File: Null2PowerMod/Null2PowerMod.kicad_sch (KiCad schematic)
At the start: 33 parts, among them J1 Conn_01x01, J2 USB_C_Receptacle_USB2.0, J3 Conn_01x01, J5 JST 2-PH, J6 Conn_01x01, U1 MCP73871, U2 TPS61030PWP, U3 MMUN2133LT1G

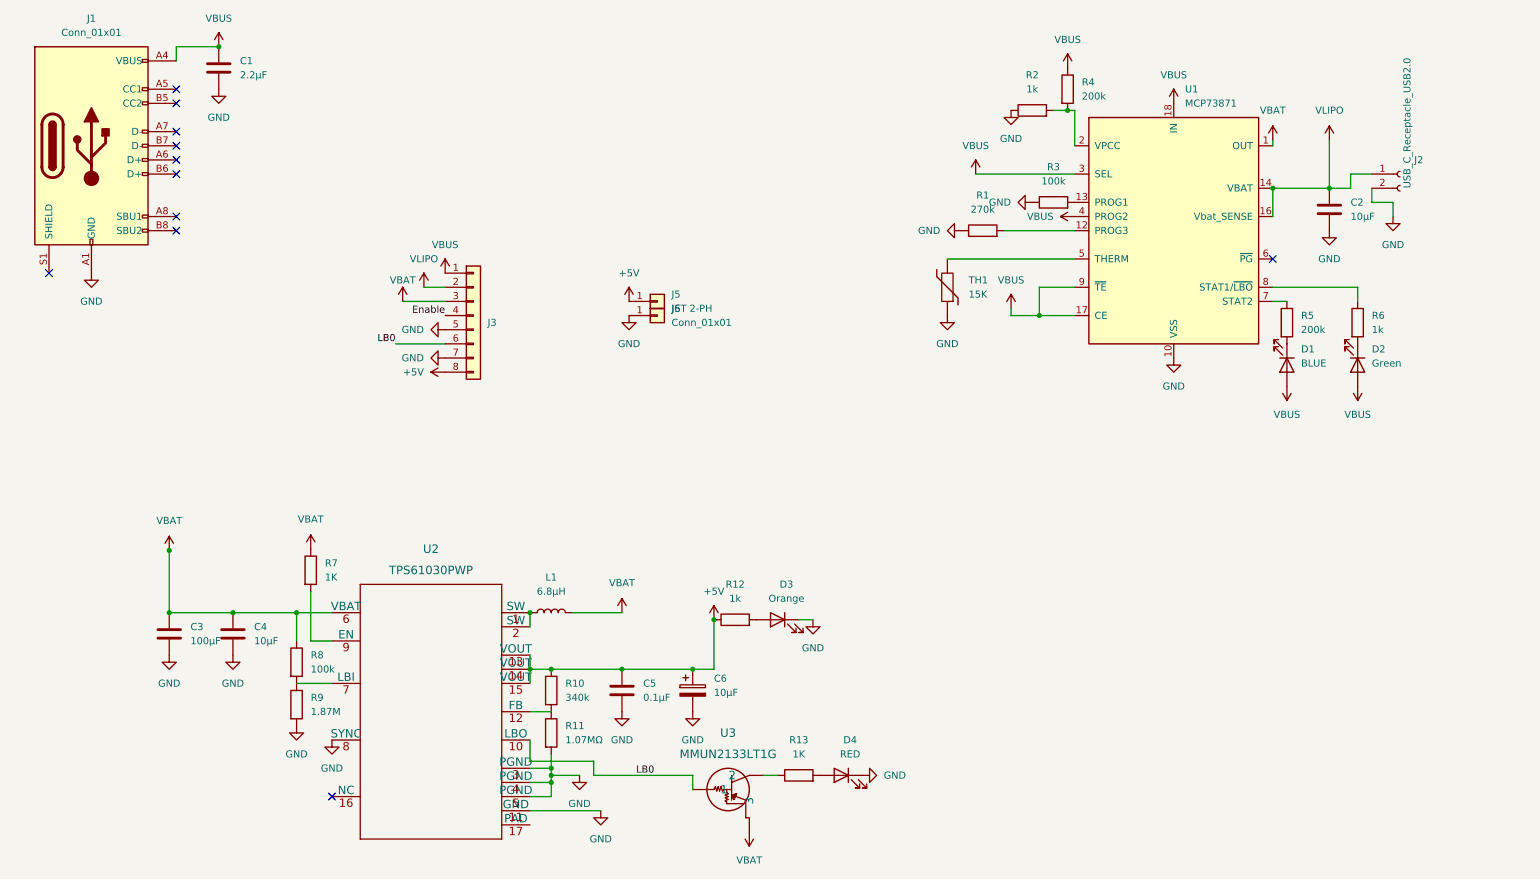
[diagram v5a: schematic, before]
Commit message: fixing power symbols
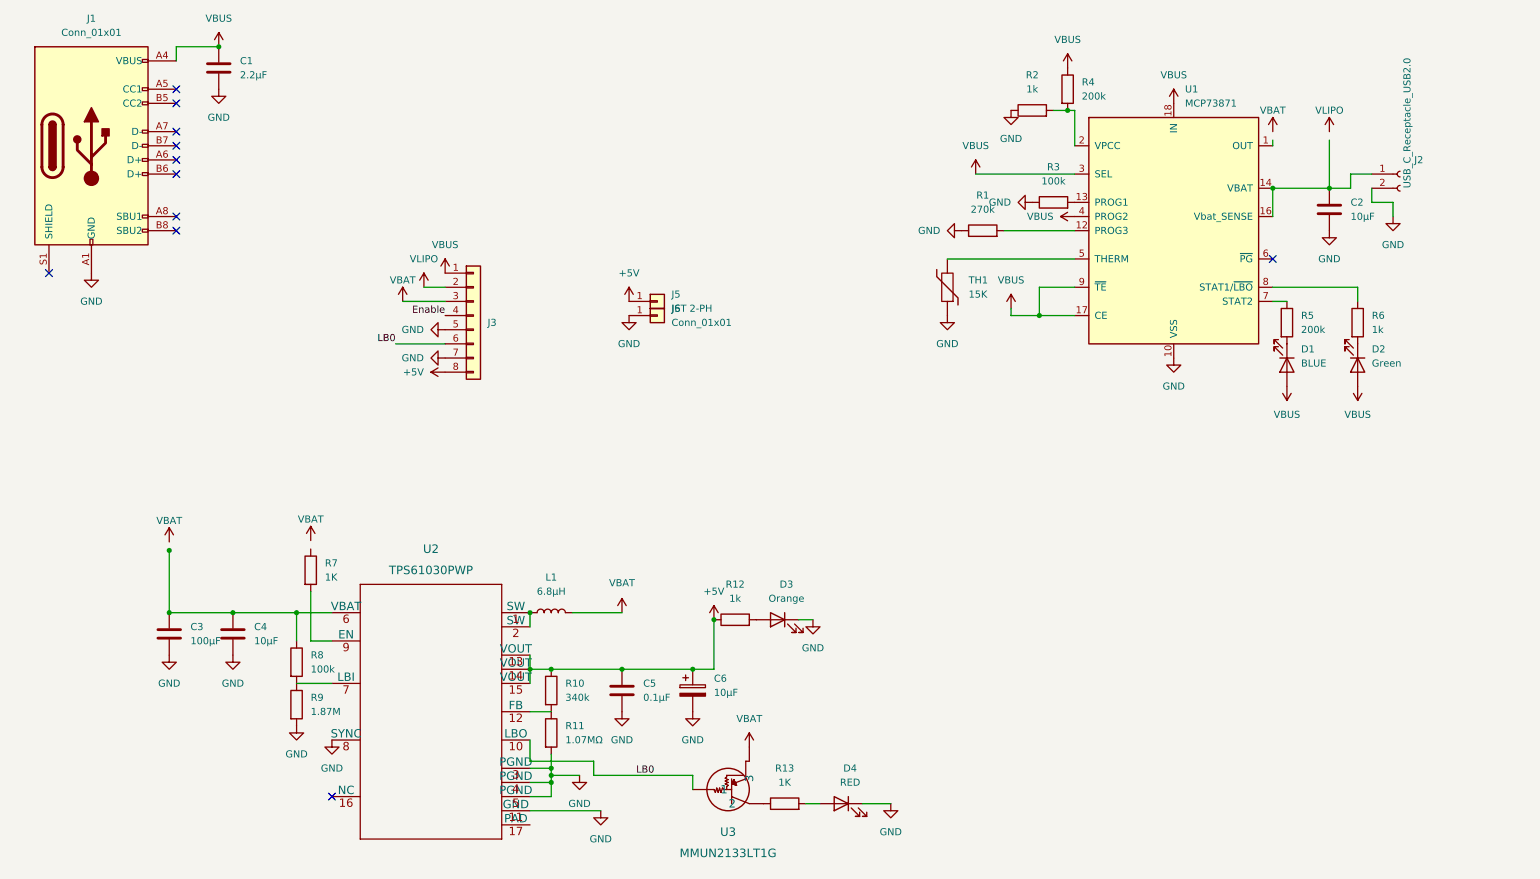
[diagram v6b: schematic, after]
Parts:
- U2: footprint TPS61030PWP:TPS61030PWP -> PWP0016K_N
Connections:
- net VBUS: now also J3.1 (Pin_1)
- net VLIPO: no longer C2.1, C3.1, C4.1, J2.1 (Pin_1), J3.1 (Pin_1), J3.3 (Pin_3), L1.2, R7.1, R8.1, U1.1 (OUT), U1.14 (VBAT), U1.15 (VBAT), U1.16 (Vbat_SENSE), U1.20 (OUT), U2.6 (VBAT), U3.3
- new net: C3.1, C4.1, R8.1, U2.6 (VBAT)
- new net: C2.1, J2.1 (Pin_1), U1.14 (VBAT), U1.15 (VBAT), U1.16 (Vbat_SENSE)
- new net: U1.1 (OUT), U1.20 (OUT)
- new net VBAT: J3.3 (Pin_3), L1.2, U3.3
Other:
- moved on the sheet: D4, R13, U3
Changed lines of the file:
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@@
   (no_connect (at 19.05 60.96))
   (no_connect (at 69.85 154.94))
-  (wire (pts (xy 149.86 151.13) (xy 147.32 151.13))
-    (stroke (width 0) (type default) (color 0 0 0 0))
-  )
   (wire (pts (xy 41.91 20.32) (xy 49.53 20.32))
     (stroke (width 0) (type default) (color 0 0 0 0))
@@
     (stroke (width 0) (type default) (color 0 0 0 0))
   )
+  (wire (pts (xy 154.94 156.21) (xy 157.48 156.21))
+    (stroke (width 0) (type default) (color 0 0 0 0))
+  )
   (wire (pts (xy 63.5 127) (xy 63.5 121.92))
     (stroke (width 0) (type default) (color 0 0 0 0))
@@
   )
   (wire (pts (xy 109.22 149.86) (xy 105.41 149.86))
+    (stroke (width 0) (type default) (color 0 0 0 0))
+  )
+  (wire (pts (xy 165.1 156.21) (xy 170.18 156.21))
     (stroke (width 0) (type default) (color 0 0 0 0))
   )
@@
     (pin "2")
   )
-  (symbol (lib_name "VBAT_3") (lib_id "Null:VBAT") (at 144.78 161.29 180) (unit 1)
-    (in_bom yes) (on_board yes) (fields_autoplaced)
-    (property "Reference" "#PWR038" (id 0) (at 149.606 163.576 0)
-      (effects (font (size 1.27 1.27)) hide)
-    )
-    (property "Value" "VBAT" (id 1) (at 144.78 166.37 0))
-    (property "Footprint" "" (id 2) (at 144.272 163.83 0)
-      (effects (font (size 1.27 1.27)) hide)
-    )
-    (property "Datasheet" "" (id 3) (at 144.272 163.83 0)
+  (symbol (lib_name "VBAT_3") (lib_id "Null:VBAT") (at 144.78 146.05 0) (unit 1)
+    (in_bom yes) (on_board yes) (fields_autoplaced)
+    (property "Reference" "#PWR038" (id 0) (at 139.954 143.764 0)
+      (effects (font (size 1.27 1.27)) hide)
+    )
+    (property "Value" "VBAT" (id 1) (at 144.78 140.97 0))
+    (property "Footprint" "" (id 2) (at 145.288 143.51 0)
+      (effects (font (size 1.27 1.27)) hide)
+    )
+    (property "Datasheet" "" (id 3) (at 145.288 143.51 0)
       (effects (font (size 1.27 1.27)) hide)
     )
@@
     (pin "2")
   )
-  (symbol (lib_id "2022-03-19_03-31-40:MMUN2133LT1G") (at 134.62 153.67 0) (unit 1)
-    (in_bom yes) (on_board yes) (fields_autoplaced)
-    (property "Reference" "U3" (id 0) (at 140.97 143.51 0)
+  (symbol (lib_id "2022-03-19_03-31-40:MMUN2133LT1G") (at 134.62 153.67 0) (mirror x) (unit 1)
+    (in_bom yes) (on_board yes) (fields_autoplaced)
+    (property "Reference" "U3" (id 0) (at 140.97 161.29 0)
       (effects (font (size 1.524 1.524)))
     )
-    (property "Value" "MMUN2133LT1G" (id 1) (at 140.97 147.32 0)
+    (property "Value" "MMUN2133LT1G" (id 1) (at 140.97 165.1 0)
       (effects (font (size 1.524 1.524)))
     )
-    (property "Footprint" "SOT_33LT1G_ONS" (id 2) (at 146.05 160.274 0)
+    (property "Footprint" "SOT_33LT1G_ONS" (id 2) (at 146.05 147.066 0)
       (effects (font (size 1.524 1.524)) hide)
     )
@@
     (pin "2")
   )
-  (symbol (lib_id "Device:LED") (at 161.29 151.13 0) (mirror y) (unit 1)
-    (in_bom yes) (on_board yes) (fields_autoplaced)
-    (property "Reference" "D4" (id 0) (at 162.8775 144.78 0))
-    (property "Value" "RED" (id 1) (at 162.8775 147.32 0))
-    (property "Footprint" "LED_SMD:LED_0201_0603Metric" (id 2) (at 161.29 151.13 0)
-      (effects (font (size 1.27 1.27)) hide)
-    )
-    (property "Datasheet" "~" (id 3) (at 161.29 151.13 0)
+  (symbol (lib_id "Device:LED") (at 161.29 156.21 0) (mirror y) (unit 1)
+    (in_bom yes) (on_board yes) (fields_autoplaced)
+    (property "Reference" "D4" (id 0) (at 162.8775 149.86 0))
+    (property "Value" "RED" (id 1) (at 162.8775 152.4 0))
+    (property "Footprint" "LED_SMD:LED_0201_0603Metric" (id 2) (at 161.29 156.21 0)
+      (effects (font (size 1.27 1.27)) hide)
+    )
+    (property "Datasheet" "~" (id 3) (at 161.29 156.21 0)
       (effects (font (size 1.27 1.27)) hide)
     )
@@
     (pin "1")
   )
-  (symbol (lib_id "Null:VBAT") (at 66.04 108.966 0) (unit 1)
+  (symbol (lib_name "VBAT_5") (lib_id "Null:VBAT") (at 66.04 108.966 0) (unit 1)
     (in_bom yes) (on_board yes) (fields_autoplaced)
     (property "Reference" "#PWR022" (id 0) (at 61.214 106.68 0)
@@
       (effects (font (size 1.524 1.524)))
     )
-    (property "Footprint" "TPS61030PWP:TPS61030PWP" (id 2) (at 87.63 141.224 0)
+    (property "Footprint" "PWP0016K_N" (id 2) (at 87.63 141.224 0)
       (effects (font (size 1.524 1.524)) hide)
     )
@@
     (pin "9")
   )
-  (symbol (lib_id "Device:R") (at 153.67 151.13 90) (unit 1)
-    (in_bom yes) (on_board yes) (fields_autoplaced)
-    (property "Reference" "R13" (id 0) (at 153.67 144.78 90))
-    (property "Value" "1K" (id 1) (at 153.67 147.32 90))
-    (property "Footprint" "Resistor_SMD:R_0201_0603Metric" (id 2) (at 153.67 152.908 90)
-      (effects (font (size 1.27 1.27)) hide)
-    )
-    (property "Datasheet" "~" (id 3) (at 153.67 151.13 0)
+  (symbol (lib_id "Device:R") (at 151.13 156.21 90) (unit 1)
+    (in_bom yes) (on_board yes) (fields_autoplaced)
+    (property "Reference" "R13" (id 0) (at 151.13 149.86 90))
+    (property "Value" "1K" (id 1) (at 151.13 152.4 90))
+    (property "Footprint" "Resistor_SMD:R_0201_0603Metric" (id 2) (at 151.13 157.988 90)
+      (effects (font (size 1.27 1.27)) hide)
+    )
+    (property "Datasheet" "~" (id 3) (at 151.13 156.21 0)
       (effects (font (size 1.27 1.27)) hide)
     )
@@
     (pin "1")
   )
-  (symbol (lib_id "Null:VBAT") (at 40.64 109.22 0) (unit 1)
+  (symbol (lib_name "VBAT_4") (lib_id "Null:VBAT") (at 40.64 109.22 0) (unit 1)
     (in_bom yes) (on_board yes) (fields_autoplaced)
     (property "Reference" "#PWR020" (id 0) (at 35.814 106.934 0)
@@
     (pin "2")
   )
-  (symbol (lib_id "power:GND") (at 165.1 151.13 90) (unit 1)
-    (in_bom yes) (on_board yes) (fields_autoplaced)
-    (property "Reference" "#PWR041" (id 0) (at 171.45 151.13 0)
-      (effects (font (size 1.27 1.27)) hide)
-    )
-    (property "Value" "GND" (id 1) (at 168.91 151.1299 90)
-      (effects (font (size 1.27 1.27)) (justify right))
-    )
-    (property "Footprint" "" (id 2) (at 165.1 151.13 0)
-      (effects (font (size 1.27 1.27)) hide)
-    )
-    (property "Datasheet" "" (id 3) (at 165.1 151.13 0)
+  (symbol (lib_id "power:GND") (at 170.18 156.21 0) (unit 1)
+    (in_bom yes) (on_board yes) (fields_autoplaced)
+    (property "Reference" "#PWR041" (id 0) (at 170.18 162.56 0)
+      (effects (font (size 1.27 1.27)) hide)
+    )
+    (property "Value" "GND" (id 1) (at 170.18 161.29 0))
+    (property "Footprint" "" (id 2) (at 170.18 156.21 0)
+      (effects (font (size 1.27 1.27)) hide)
+    )
+    (property "Datasheet" "" (id 3) (at 170.18 156.21 0)
       (effects (font (size 1.27 1.27)) hide)
     )
@@
     )
     (path "/c6b48e28-7371-4b57-8db2-ddb38d25233c"
-      (reference "U2") (unit 1) (value "TPS61030PWP") (footprint "TPS61030PWP:TPS61030PWP")
+      (reference "U2") (unit 1) (value "TPS61030PWP") (footprint "PWP0016K_N")
     )
     (path "/3f63a2b0-b68f-4f63-9d5f-f5ce53b75bec"

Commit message: wtf happened to the schematic?
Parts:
- U2: footprint PWP0016K_N -> TPS61030PWP:TPS61030PWP
- U3: footprint SOT_33LT1G_ONS -> MMUN2133LT1G:MMUN2133LT1G
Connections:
- net GND: now also U2.17 (PAD)
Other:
- moved on the sheet: J6
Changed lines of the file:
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@@
   (junction (at 238.76 45.72) (diameter 0) (color 0 0 0 0)
-  )
-  (junction (at 40.64 110.744) (diameter 0) (color 0 0 0 0)
   )
   (junction (at 134.62 132.08) (diameter 0) (color 0 0 0 0)
@@
     (stroke (width 0) (type default) (color 0 0 0 0))
   )
-  (wire (pts (xy 40.64 110.744) (xy 40.64 121.92))
+  (wire (pts (xy 40.64 110.49) (xy 40.64 121.92))
     (stroke (width 0) (type default) (color 0 0 0 0))
   )
@@
   )
   (wire (pts (xy 254 63.5) (xy 254 66.04))
-    (stroke (width 0) (type default) (color 0 0 0 0))
-  )
-  (wire (pts (xy 40.64 110.49) (xy 40.64 110.744))
     (stroke (width 0) (type default) (color 0 0 0 0))
   )
@@
     (pin "1")
   )
-  (symbol (lib_id "Connector_Generic:Conn_01x01") (at 128.27 68.58 0) (unit 1)
-    (in_bom yes) (on_board yes) (fields_autoplaced)
-    (property "Reference" "J6" (id 0) (at 130.81 67.3099 0)
-      (effects (font (size 1.27 1.27)) (justify left))
-    )
-    (property "Value" "Conn_01x01" (id 1) (at 130.81 69.8499 0)
-      (effects (font (size 1.27 1.27)) (justify left))
-    )
-    (property "Footprint" "Connector_PinHeader_2.54mm:PinHeader_1x01_P2.54mm_Vertical" (id 2) (at 128.27 68.58 0)
-      (effects (font (size 1.27 1.27)) hide)
-    )
-    (property "Datasheet" "~" (id 3) (at 128.27 68.58 0)
+  (symbol (lib_id "Connector_Generic:Conn_01x01") (at 128.27 71.12 0) (unit 1)
+    (in_bom yes) (on_board yes) (fields_autoplaced)
+    (property "Reference" "J6" (id 0) (at 130.81 69.8499 0)
+      (effects (font (size 1.27 1.27)) (justify left))
+    )
+    (property "Value" "Conn_01x01" (id 1) (at 130.81 72.3899 0)
+      (effects (font (size 1.27 1.27)) (justify left))
+    )
+    (property "Footprint" "Connector_PinHeader_2.54mm:PinHeader_1x01_P2.54mm_Vertical" (id 2) (at 128.27 71.12 0)
+      (effects (font (size 1.27 1.27)) hide)
+    )
+    (property "Datasheet" "~" (id 3) (at 128.27 71.12 0)
       (effects (font (size 1.27 1.27)) hide)
     )
@@
       (effects (font (size 1.524 1.524)))
     )
-    (property "Footprint" "SOT_33LT1G_ONS" (id 2) (at 146.05 147.066 0)
+    (property "Footprint" "MMUN2133LT1G:MMUN2133LT1G" (id 2) (at 146.05 147.066 0)
       (effects (font (size 1.524 1.524)) hide)
     )
@@
     (pin "1")
   )
+  (symbol (lib_id "power:GND") (at 105.41 160.02 0) (unit 1)
+    (in_bom yes) (on_board yes) (fields_autoplaced)
+    (property "Reference" "#PWR?" (id 0) (at 105.41 166.37 0)
+      (effects (font (size 1.27 1.27)) hide)
+    )
+    (property "Value" "GND" (id 1) (at 105.41 165.1 0))
+    (property "Footprint" "" (id 2) (at 105.41 160.02 0)
+      (effects (font (size 1.27 1.27)) hide)
+    )
+    (property "Datasheet" "" (id 3) (at 105.41 160.02 0)
+      (effects (font (size 1.27 1.27)) hide)
+    )
+    (pin "1")
+  )
   (symbol (lib_id "power:VBUS") (at 191.77 67.31 0) (unit 1)
     (in_bom yes) (on_board yes) (fields_autoplaced)
@@
     (pin "2")
   )
-  (symbol (lib_id "power:GND") (at 123.19 68.58 0) (unit 1)
-    (in_bom yes) (on_board yes) (fields_autoplaced)
-    (property "Reference" "#PWR043" (id 0) (at 123.19 74.93 0)
-      (effects (font (size 1.27 1.27)) hide)
-    )
-    (property "Value" "GND" (id 1) (at 123.19 73.66 0))
-    (property "Footprint" "" (id 2) (at 123.19 68.58 0)
-      (effects (font (size 1.27 1.27)) hide)
-    )
-    (property "Datasheet" "" (id 3) (at 123.19 68.58 0)
+  (symbol (lib_id "power:GND") (at 123.19 71.12 0) (unit 1)
+    (in_bom yes) (on_board yes) (fields_autoplaced)
+    (property "Reference" "#PWR043" (id 0) (at 123.19 77.47 0)
+      (effects (font (size 1.27 1.27)) hide)
+    )
+    (property "Value" "GND" (id 1) (at 123.19 76.2 0))
+    (property "Footprint" "" (id 2) (at 123.19 71.12 0)
+      (effects (font (size 1.27 1.27)) hide)
+    )
+    (property "Datasheet" "" (id 3) (at 123.19 71.12 0)
       (effects (font (size 1.27 1.27)) hide)
     )
@@
       (effects (font (size 1.524 1.524)))
     )
-    (property "Footprint" "PWP0016K_N" (id 2) (at 87.63 141.224 0)
+    (property "Footprint" "TPS61030PWP:TPS61030PWP" (id 2) (at 87.63 141.224 0)
       (effects (font (size 1.524 1.524)) hide)
     )
@@
       (reference "#PWR043") (unit 1) (value "GND") (footprint "")
     )
+    (path "/9d204501-9bc1-49d3-901e-dc3cce70c8f8"
+      (reference "#PWR?") (unit 1) (value "GND") (footprint "")
+    )
     (path "/65971997-ba92-4f22-b849-ff939ee9f2dc"
       (reference "C1") (unit 1) (value "2.2μF") (footprint "Capacitor_SMD:C_0201_0603Metric")
@@
     )
     (path "/c6b48e28-7371-4b57-8db2-ddb38d25233c"
-      (reference "U2") (unit 1) (value "TPS61030PWP") (footprint "PWP0016K_N")
+      (reference "U2") (unit 1) (value "TPS61030PWP") (footprint "TPS61030PWP:TPS61030PWP")
     )
     (path "/3f63a2b0-b68f-4f63-9d5f-f5ce53b75bec"
-      (reference "U3") (unit 1) (value "MMUN2133LT1G") (footprint "SOT_33LT1G_ONS")
-    )
-  )
+      (reference "U3") (unit 1) (value "MMUN2133LT1G") (footprint "MMUN2133LT1G:MMUN2133LT1G")
+    )
+  )
